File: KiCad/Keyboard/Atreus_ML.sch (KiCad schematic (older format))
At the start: 86 parts, among them K1 CHERRY_ML, K10 CHERRY_ML, K11 CHERRY_ML, K12 CHERRY_ML, K13 CHERRY_ML, K14 CHERRY_ML, K15 CHERRY_ML, K16 CHERRY_ML, K17 CHERRY_ML, K18 CHERRY_ML, K19 CHERRY_ML, K2 CHERRY_ML, K20 CHERRY_ML, K21 CHERRY_ML, K22 CHERRY_ML, K23 CHERRY_ML, K24 CHERRY_ML, K25 CHERRY_ML, K26 CHERRY_ML, K27 CHERRY_ML, K28 CHERRY_ML, K29 CHERRY_ML, K3 CHERRY_ML, K30 CHERRY_ML, K31 CHERRY_ML, K32 CHERRY_ML, K33 CHERRY_ML, K34 CHERRY_ML, K35 CHERRY_ML, K36 CHERRY_ML, K37 CHERRY_ML, K38 CHERRY_ML, K39 CHERRY_ML, K4 CHERRY_ML, K40 CHERRY_ML, K41 CHERRY_ML, K42 CHERRY_ML, K5 CHERRY_ML, K6 CHERRY_ML, K7 CHERRY_ML, K8 CHERRY_ML, K9 CHERRY_ML, P1 CONN_01X07, U1 TEENSY2.0

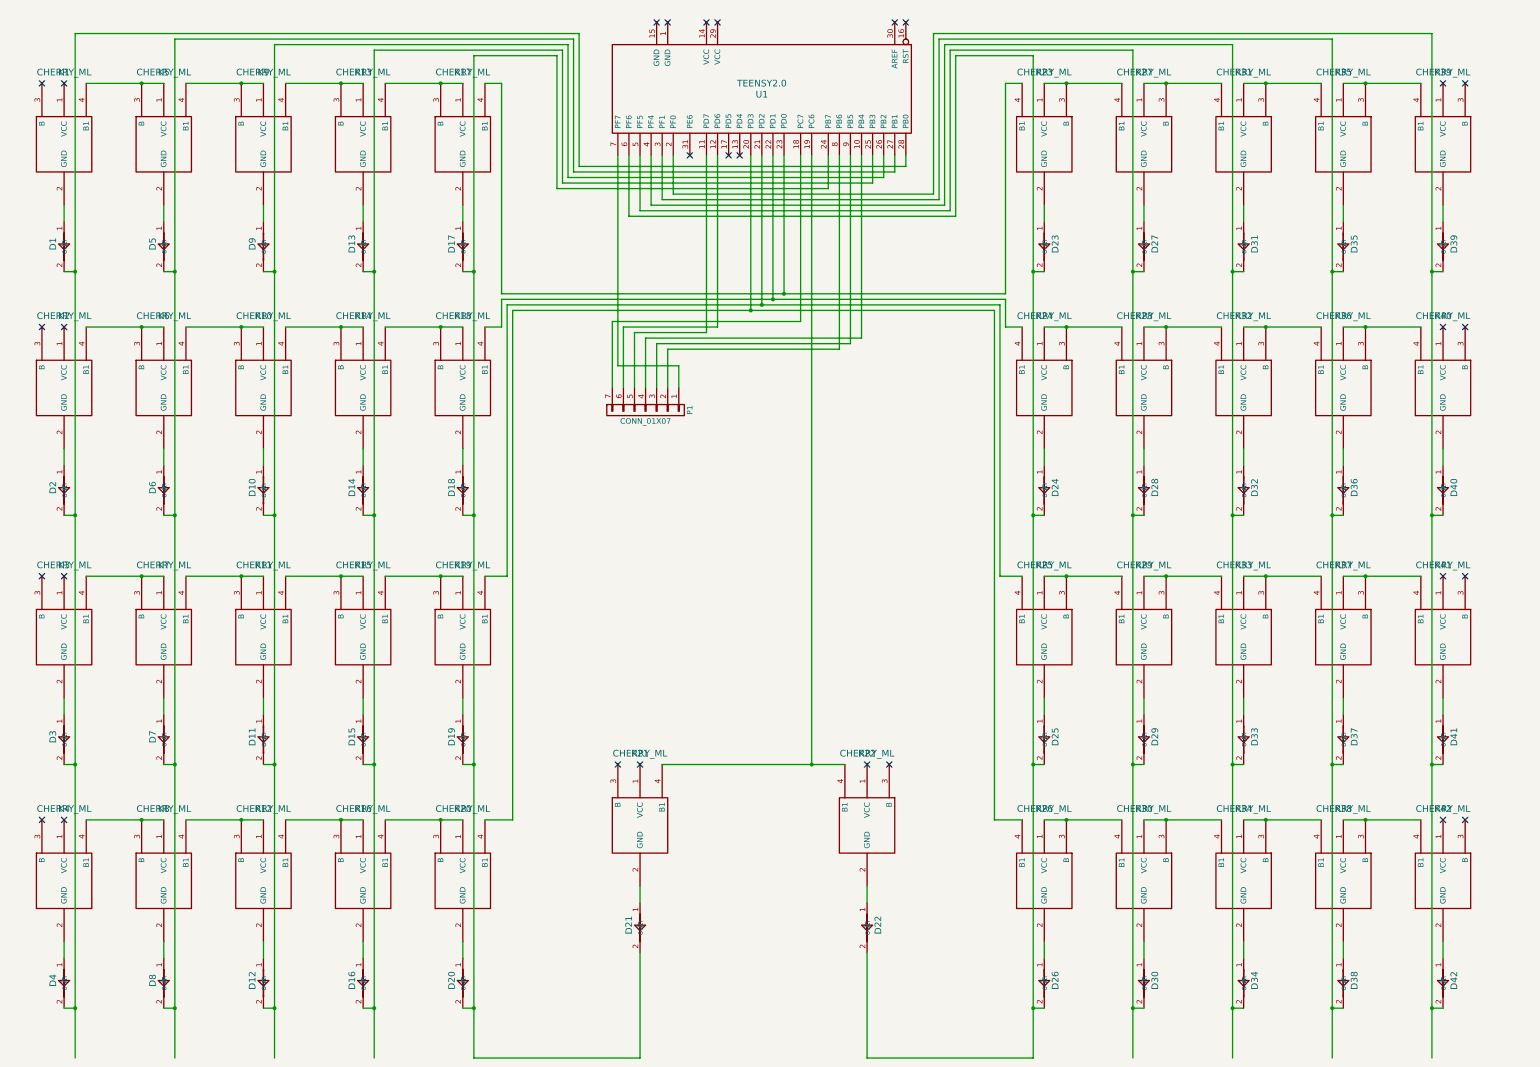
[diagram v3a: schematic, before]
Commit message: Fixed logical layout, starting physical
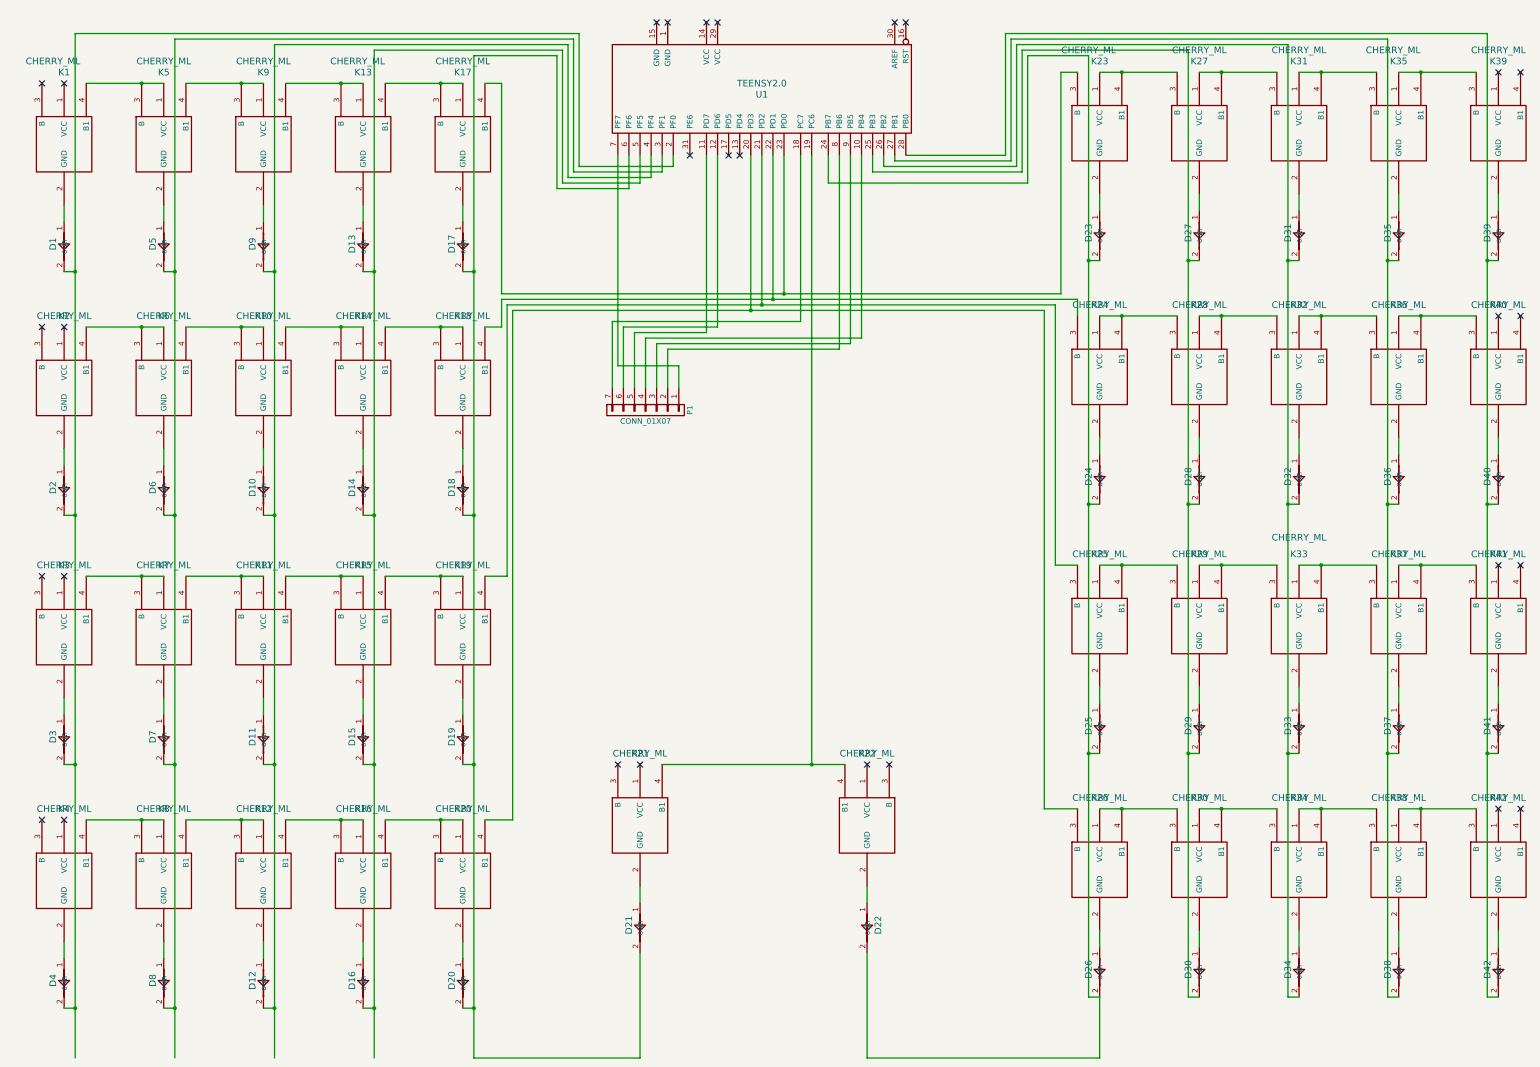
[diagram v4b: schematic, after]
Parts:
- D1, D10, D11, D12, D13, D14, D15, D16, D17, D18, D19, D2, D20, D21, D22, D23, D24, D25, D26, D27, D28, D29, D3, D30, D31, D32, D33, D34, D35, D36, D37, D38, D39, D4, D40, D41, D42, D5, D6, D7, D8, D9: footprint (none) -> 4148_rev2:4148_rev2
- K1, K10, K11, K12, K13, K14, K15, K16, K17, K18, K19, K2, K20, K21, K22, K23, K24, K25, K26, K27, K28, K29, K3, K30, K31, K32, K33, K34, K35, K36, K37, K38, K39, K4, K40, K41, K42, K5, K6, K7, K8, K9: footprint (none) -> CHERRY_ML:CHERRY_ML
- P1: footprint (none) -> Socket_Strips:Socket_Strip_Straight_1x07
- U1: footprint (none) -> Teensy:TEENSY_2.0
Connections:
- wire segments 215 -> 214

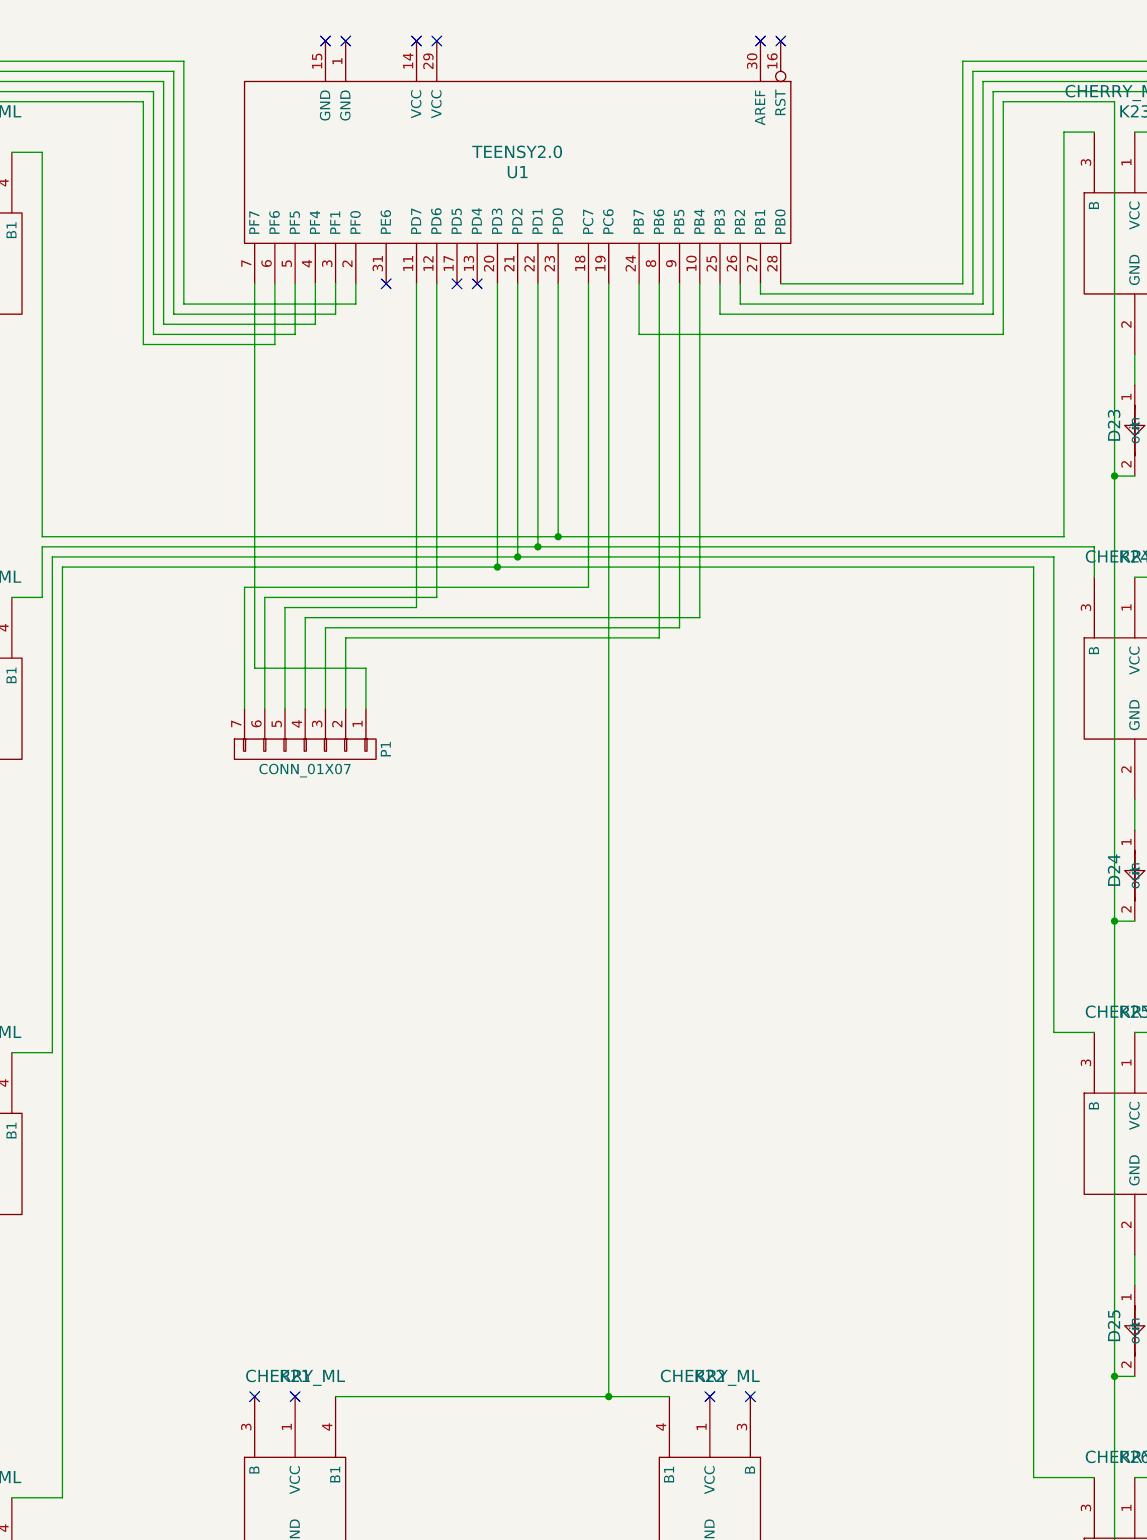
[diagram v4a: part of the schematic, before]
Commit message: Switching to teensu compact
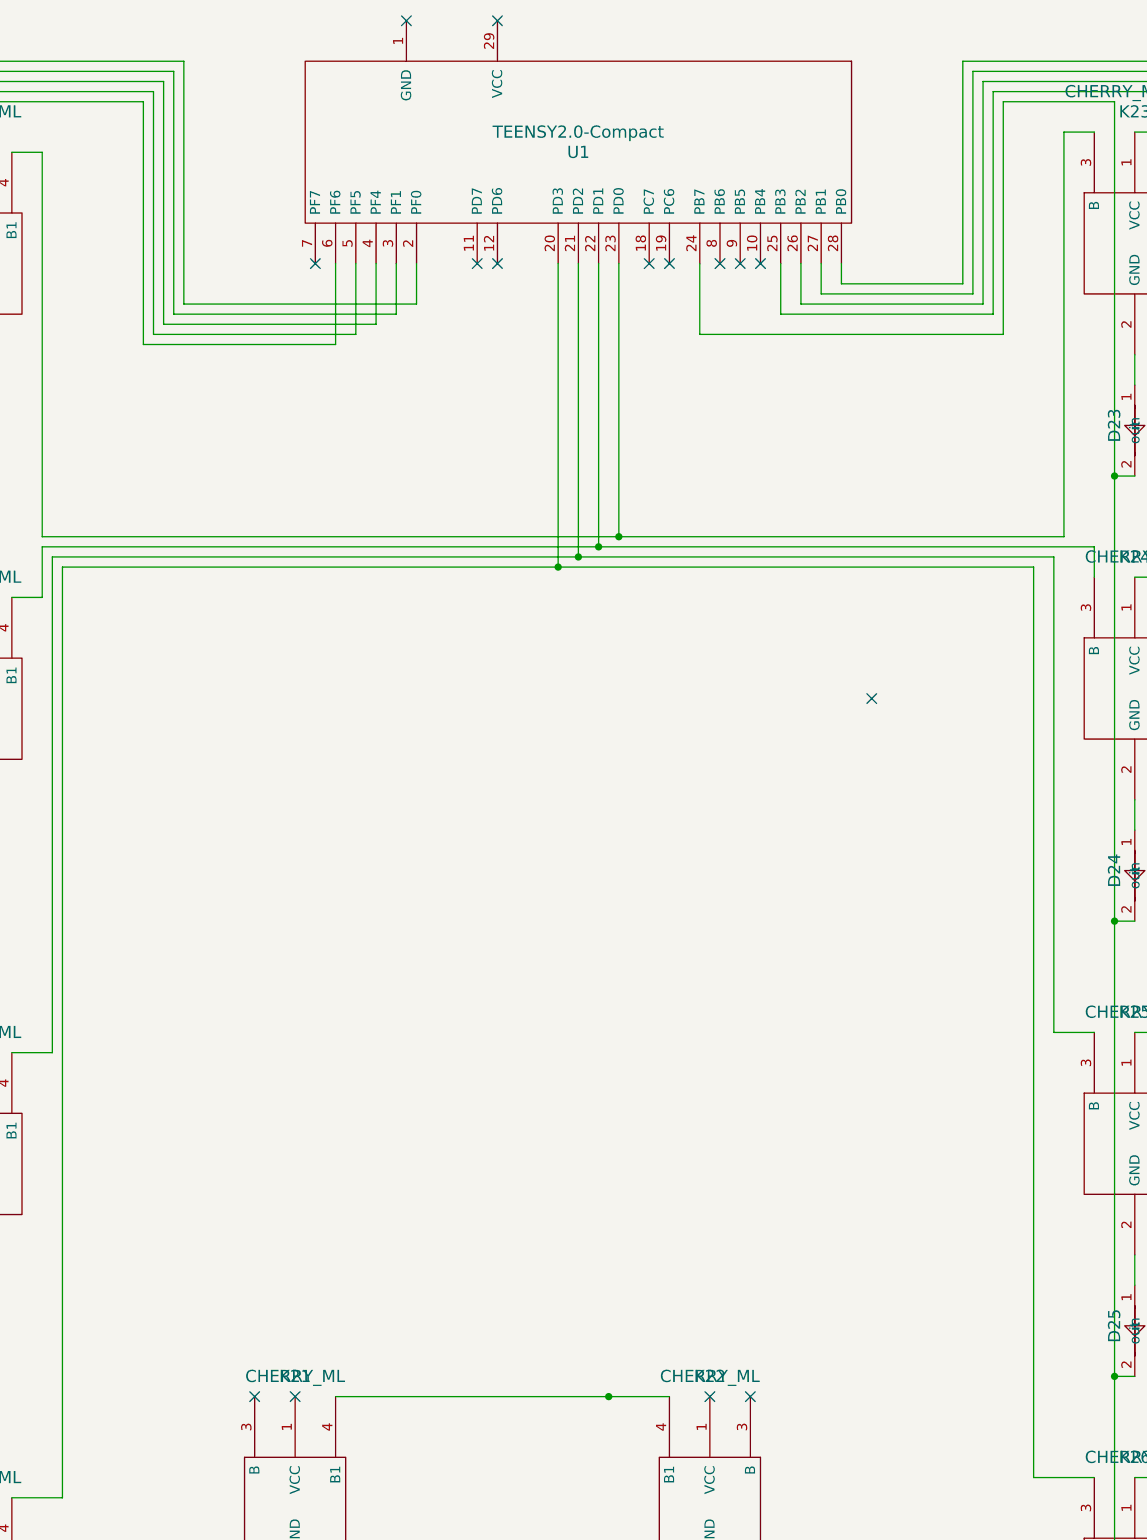
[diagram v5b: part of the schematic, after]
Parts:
- removed P1: CONN_01X07, Socket_Strips:Socket_Strip_Straight_1x07, symbol CONN_01X07
- removed U1: TEENSY2.0, Teensy:TEENSY_2.0, symbol TEENSY2.0
- added U1: TEENSY2.0-Compact, Teensy:TEENSY_2.0-Compact, symbol TEENSY2.0-Compact
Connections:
- net at K17.4 (B1), K23.3 (B): now also U1.23 (PD0)
- net at D1.2 (out), D2.2 (out), D3.2 (out)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: now also U1.2 (PF0)
- net at D5.2 (out), D6.2 (out), D7.2 (out)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: now also U1.3 (PF1)
- net at D10.2 (out), D11.2 (out), D12.2 (out)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: now also U1.4 (PF4)
- net at D13.2 (out), D14.2 (out), D15.2 (out)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: now also U1.5 (PF5)
- net at D17.2 (out), D18.2 (out), D19.2 (out)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: now also U1.6 (PF6)
- net at K18.4 (B1), K24.3 (B): now also U1.22 (PD1)
- net at K19.4 (B1), K25.3 (B): now also U1.21 (PD2)
- net at K20.4 (B1), K26.3 (B): now also U1.20 (PD3)
- net at D22.2 (out), D23.2 (out), D24.2 (out)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: now also U1.24 (PB7)
- net at D27.2 (out), D28.2 (out), D29.2 (out)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: now also U1.25 (PB3)
- net at D31.2 (out), D32.2 (out), D33.2 (out)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: now also U1.26 (PB2)
- net at D35.2 (out), D36.2 (out), D37.2 (out)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: now also U1.27 (PB1)
- net at D39.2 (out), D40.2 (out), D41.2 (out)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: now also U1.28 (PB0)
- no-connect marks 29 -> 31
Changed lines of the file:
@@
 NoConn ~ 1950 1200
 NoConn ~ 2150 1200
-NoConn ~ 9750 650
-NoConn ~ 9650 650
-NoConn ~ 8050 650
-NoConn ~ 7950 650
-NoConn ~ 7600 650
-NoConn ~ 7500 650
 $Comp
 L CHERRY_ML K22
@@
 NoConn ~ 9400 7350
 $Comp
-L TEENSY2.0 U1
-U 1 1 56DE575B
-P 8450 1250
-F 0 "U1" V 8500 1250 60  0000 C CNN
-F 1 "TEENSY2.0" V 8400 1250 60  0000 C CNN
-F 2 "Teensy:TEENSY_2.0" H 8450 1250 60  0001 C CNN
-F 3 "" H 8450 1250 60  0000 C CNN
-	1    8450 1250
-	0    1    1    0
-$EndComp
-$Comp
-L CONN_01X07 P1
-U 1 1 56F91115
-P 7400 4150
-F 0 "P1" H 7400 4550 50  0000 C CNN
-F 1 "CONN_01X07" V 7500 4150 50  0000 C CNN
-F 2 "Socket_Strips:Socket_Strip_Straight_1x07" H 7400 4150 50  0001 C CNN
-F 3 "" H 7400 4150 50  0000 C CNN
-	1    7400 4150
-	0    1    1    0
-$EndComp
-NoConn ~ 7800 1850
-NoConn ~ 8150 1850
-NoConn ~ 8250 1850
-$Comp
 L CHERRY_ML K23
 U 1 1 56F9BB37
@@
 Wire Wire Line
 	6600 950  6600 2150
-Wire Wire Line
-	8650 1850 8650 3100
-Connection ~ 8650 3100
-Wire Wire Line
-	8550 1850 8550 3150
-Connection ~ 8550 3150
-Wire Wire Line
-	8450 1850 8450 3200
-Connection ~ 8450 3200
-Wire Wire Line
-	8350 1850 8350 3250
-Connection ~ 8350 3250
-Wire Wire Line
-	8900 1850 8900 7350
 Connection ~ 8900 7350
-Wire Wire Line
-	7150 1850 7150 3750
-Wire Wire Line
-	7150 3750 7700 3750
-Wire Wire Line
-	7700 3750 7700 3950
-Wire Wire Line
-	9150 1850 9150 3600
-Wire Wire Line
-	9150 3600 7600 3600
-Wire Wire Line
-	7600 3600 7600 3950
-Wire Wire Line
-	9250 1850 9250 3550
-Wire Wire Line
-	9250 3550 7500 3550
-Wire Wire Line
-	7500 3550 7500 3950
-Wire Wire Line
-	9350 1850 9350 3500
-Wire Wire Line
-	9350 3500 7400 3500
-Wire Wire Line
-	7400 3500 7400 3950
-Wire Wire Line
-	7950 1850 7950 3450
-Wire Wire Line
-	7950 3450 7300 3450
-Wire Wire Line
-	7300 3450 7300 3950
-Wire Wire Line
-	8050 1850 8050 3400
-Wire Wire Line
-	8050 3400 7200 3400
-Wire Wire Line
-	7200 3400 7200 3950
-Wire Wire Line
-	8800 1850 8800 3350
-Wire Wire Line
-	8800 3350 7100 3350
-Wire Wire Line
-	7100 3350 7100 3950
 Wire Wire Line
 	11500 2200 11500 2350
@@
 Wire Wire Line
 	11000 7750 11000 3250
-Wire Wire Line
-	7650 1850 7650 1950
-Wire Wire Line
-	7650 1950 6800 1950
-Wire Wire Line
-	7550 1850 7550 2000
-Wire Wire Line
-	7550 2000 6750 2000
-Wire Wire Line
-	7450 1850 7450 2050
-Wire Wire Line
-	7450 2050 6700 2050
-Wire Wire Line
-	7350 1850 7350 2100
-Wire Wire Line
-	7350 2100 6650 2100
-Wire Wire Line
-	7250 1850 7250 2150
-Wire Wire Line
-	7250 2150 6600 2150
-Wire Wire Line
-	10650 1850 9750 1850
-Wire Wire Line
-	9650 1850 9650 1900
-Wire Wire Line
-	9650 1900 10700 1900
-Wire Wire Line
-	9550 1850 9550 1950
-Wire Wire Line
-	9550 1950 10750 1950
-Wire Wire Line
-	10800 2000 9450 2000
-Wire Wire Line
-	9450 2000 9450 1850
-Wire Wire Line
-	9050 1850 9050 2100
-Wire Wire Line
-	9050 2100 10850 2100
 NoConn ~ 15300 1100
 NoConn ~ 15100 1100
@@
 Wire Wire Line
 	11500 10000 11500 9450
+$Comp
+L TEENSY2.0-Compact U1
+U 1 1 56FBFB10
+P 8750 1150
+F 0 "U1" V 8800 1150 60  0000 C CNN
+F 1 "TEENSY2.0-Compact" V 8700 1150 60  0000 C CNN
+F 2 "Teensy:TEENSY_2.0-Compact" H 8750 1150 60  0001 C CNN
+F 3 "" H 8750 1150 60  0000 C CNN
+	1    8750 1150
+	0    1    1    0
+$EndComp
+Wire Wire Line
+	10650 1850 10050 1850
+Wire Wire Line
+	10050 1850 10050 1750
+Wire Wire Line
+	10700 1900 9950 1900
+Wire Wire Line
+	9950 1900 9950 1750
+Wire Wire Line
+	10750 1950 9850 1950
+Wire Wire Line
+	9850 1950 9850 1750
+Wire Wire Line
+	10800 2000 9750 2000
+Wire Wire Line
+	9750 2000 9750 1750
+Wire Wire Line
+	10850 2100 9350 2100
+Wire Wire Line
+	9350 2100 9350 1750
+Wire Wire Line
+	6800 1950 7950 1950
+Wire Wire Line
+	7950 1950 7950 1750
+Wire Wire Line
+	6750 2000 7850 2000
+Wire Wire Line
+	7850 2000 7850 1750
+Wire Wire Line
+	6700 2050 7750 2050
+Wire Wire Line
+	7750 2050 7750 1750
+Wire Wire Line
+	6650 2100 7650 2100
+Wire Wire Line
+	7650 2100 7650 1750
+Wire Wire Line
+	6600 2150 7550 2150
+Wire Wire Line
+	7550 2150 7550 1750
+Wire Wire Line
+	8950 1750 8950 3100
+Connection ~ 8950 3100
+Wire Wire Line
+	8850 1750 8850 3150
+Connection ~ 8850 3150
+Wire Wire Line
+	8750 1750 8750 3200
+Connection ~ 8750 3200
+Wire Wire Line
+	8650 1750 8650 3250
+Connection ~ 8650 3250
+NoConn ~ 9200 1750
+NoConn ~ 9450 1750
+NoConn ~ 9550 1750
+NoConn ~ 9650 1750
+NoConn ~ 8350 1750
+NoConn ~ 8250 1750
+NoConn ~ 7450 1750
+NoConn ~ 7900 550
+NoConn ~ 8350 550
+NoConn ~ 9100 1750
+NoConn ~ 10200 3900
 $EndSCHEMATC

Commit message: Layout done!
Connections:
- net at K21.4 (B1): now also K22.3 (B), U1.19 (PC6); no longer K22.4 (B1)
- no-connect marks 31 -> 30
